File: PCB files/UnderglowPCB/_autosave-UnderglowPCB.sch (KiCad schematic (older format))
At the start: 67 parts, among them J1 USB_B_Micro, J12 DB9_Male, J4 Conn_01x07, J5 Conn_01x05, J7 Screw_Terminal_01x03, J8 Screw_Terminal_01x03, Q1 S8050, Q2 S8050, SW1 SW_Push, U1 CP2102N-A01-GQFN28, U2 TPS62133, U3 74HC14, U4 74HC14, U5 LD56100DPU33R, U6 ESP32-WROOM-32D, U7 SN65HVD230, U8 USBLC6-2SC6

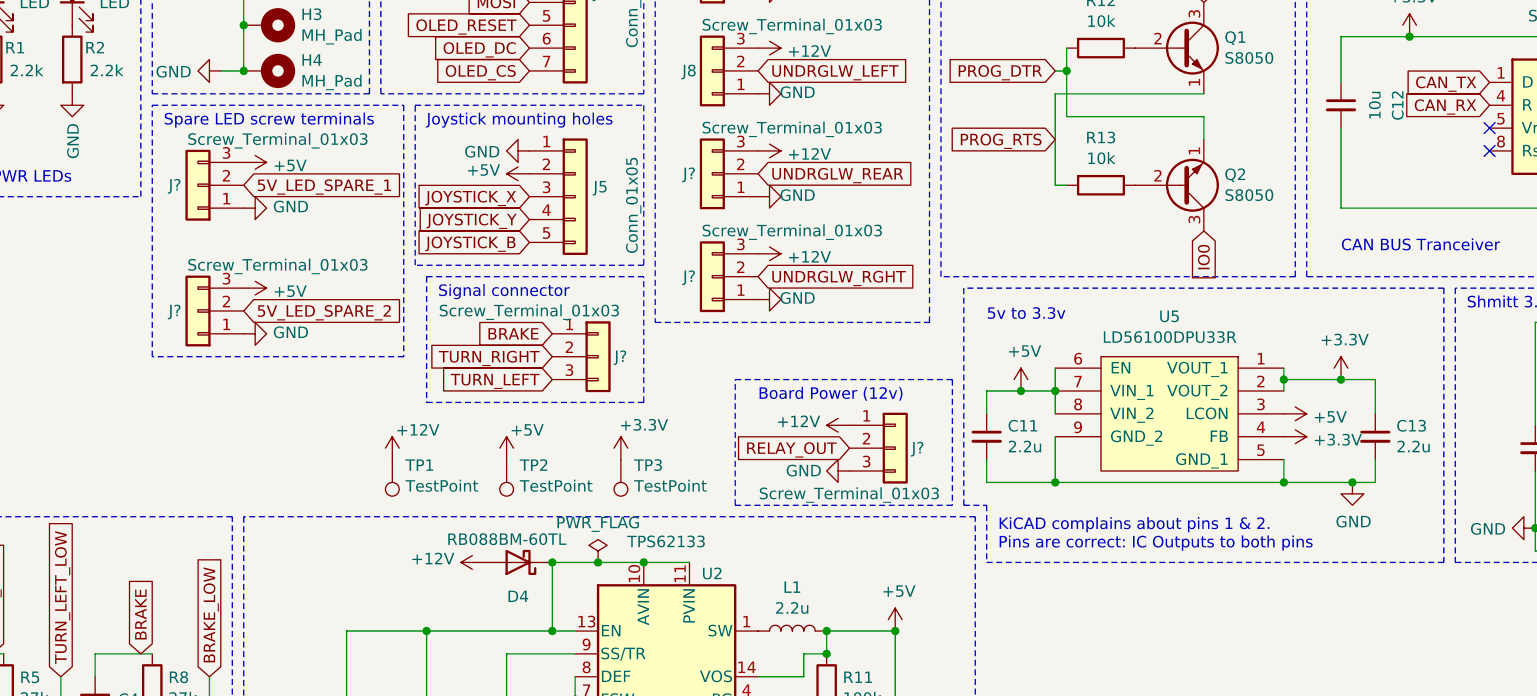
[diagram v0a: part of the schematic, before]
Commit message: Schemtic refined, removed screw terminals, added USB ESD prtection, test points, adjusted paths.
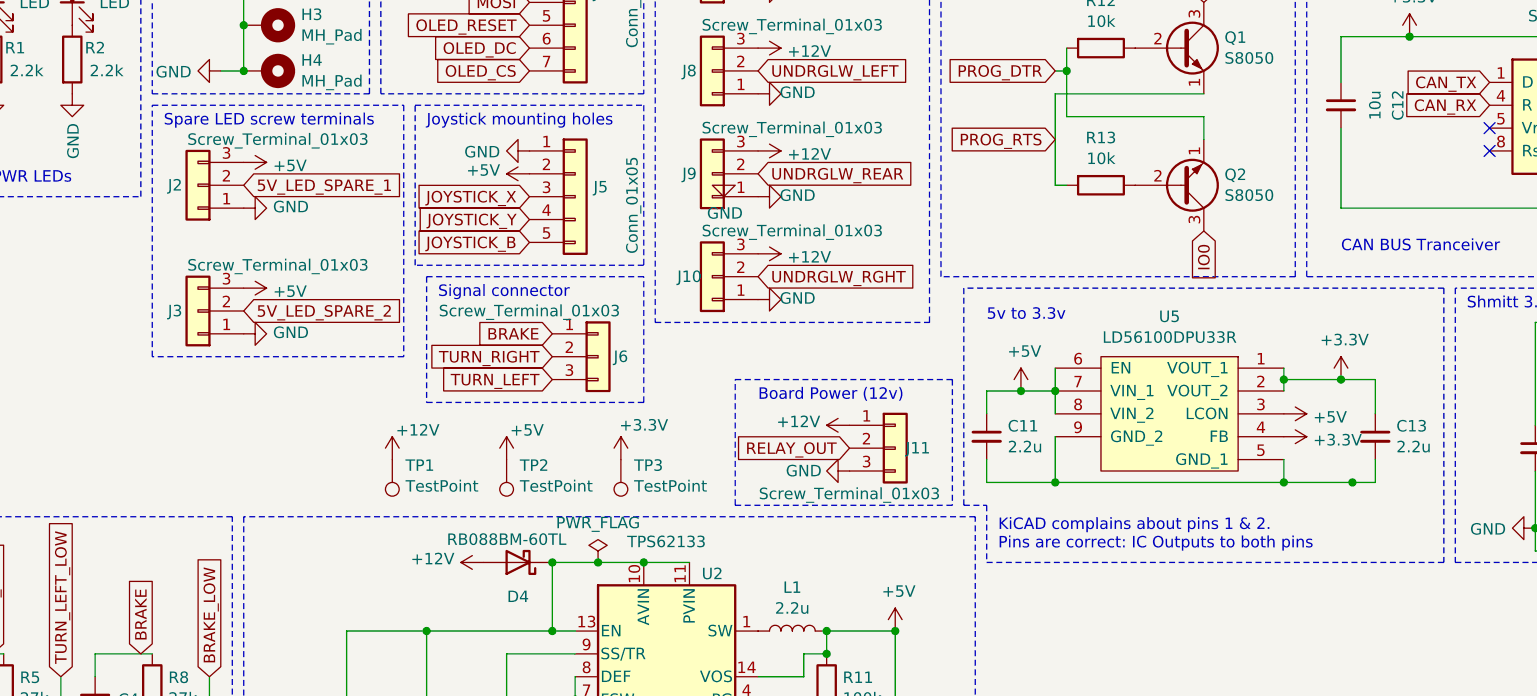
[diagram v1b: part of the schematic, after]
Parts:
- J10, J11, J3, J6, J9: renamed from J?; footprint TerminalBlock_Phoenix:TerminalBlock_Phoenix_MKDS-1,5-3-5.08_1x03_P5.08mm_Horizontal -> Connector_PinHeader_2.54mm:PinHeader_1x03_P2.54mm_Vertical
- J2: renamed from J?; footprint TerminalBlock_Phoenix:TerminalBlock_Phoenix_MKDS-1,5-3-5.08_1x03_P5.08mm_Horizontal -> Connector_PinSocket_2.54mm:PinSocket_1x03_P2.54mm_Vertical
- J7, J8: footprint TerminalBlock_Phoenix:TerminalBlock_Phoenix_MKDS-1,5-3-5.08_1x03_P5.08mm_Horizontal -> Connector_PinHeader_2.54mm:PinHeader_1x03_P2.54mm_Vertical
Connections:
- net GND: no longer C11.2, C13.2, U5.5 (GND_1), U5.9 (GND_2)
- new net: C11.2, C13.2, U5.5 (GND_1), U5.9 (GND_2)
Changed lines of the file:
@@
 L power:GND #PWR017
 U 1 1 606E5808
-P 7900 6400
-F 0 "#PWR017" H 7900 6150 50  0001 C CNN
-F 1 "GND" H 7905 6227 50  0000 C CNN
-F 2 "" H 7900 6400 50  0001 C CNN
-F 3 "" H 7900 6400 50  0001 C CNN
-	1    7900 6400
+P 5150 5050
+F 0 "#PWR017" H 5150 4800 50  0001 C CNN
+F 1 "GND" H 5155 4877 50  0000 C CNN
+F 2 "" H 5150 5050 50  0001 C CNN
+F 3 "" H 5150 5050 50  0001 C CNN
+	1    5150 5050
 	1    0    0    -1
 $EndComp
@@
 F 0 "J7" H 5200 4150 50  0000 C CNN
 F 1 "Screw_Terminal_01x03" H 4750 3950 50  0000 C CNN
-F 2 "TerminalBlock_Phoenix:TerminalBlock_Phoenix_MKDS-1,5-3-5.08_1x03_P5.08mm_Horizontal" H 5100 4150 50  0001 C CNN
+F 2 "Connector_PinHeader_2.54mm:PinHeader_1x03_P2.54mm_Vertical" H 5100 4150 50  0001 C CNN
 F 3 "~" H 5100 4150 50  0001 C CNN
 	1    5100 4150
@@
 F 0 "J8" H 5200 4600 50  0000 C CNN
 F 1 "Screw_Terminal_01x03" H 4750 4400 50  0000 C CNN
-F 2 "TerminalBlock_Phoenix:TerminalBlock_Phoenix_MKDS-1,5-3-5.08_1x03_P5.08mm_Horizontal" H 5100 4600 50  0001 C CNN
+F 2 "Connector_PinHeader_2.54mm:PinHeader_1x03_P2.54mm_Vertical" H 5100 4600 50  0001 C CNN
 F 3 "~" H 5100 4600 50  0001 C CNN
 	1    5100 4600
@@
 $EndComp
 $Comp
-L Connector_Generic:Conn_01x03 J?
+L Connector_Generic:Conn_01x03 J9
 U 1 1 60AA5191
 P 5100 5050
-F 0 "J?" H 5200 5050 50  0000 C CNN
+F 0 "J9" H 5200 5050 50  0000 C CNN
 F 1 "Screw_Terminal_01x03" H 4750 4850 50  0000 C CNN
-F 2 "TerminalBlock_Phoenix:TerminalBlock_Phoenix_MKDS-1,5-3-5.08_1x03_P5.08mm_Horizontal" H 5100 5050 50  0001 C CNN
+F 2 "Connector_PinHeader_2.54mm:PinHeader_1x03_P2.54mm_Vertical" H 5100 5050 50  0001 C CNN
 F 3 "~" H 5100 5050 50  0001 C CNN
 	1    5100 5050
@@
 $EndComp
 $Comp
-L Connector_Generic:Conn_01x03 J?
+L Connector_Generic:Conn_01x03 J10
 U 1 1 60AA6F94
 P 5100 5500
-F 0 "J?" H 5200 5500 50  0000 C CNN
+F 0 "J10" H 5200 5500 50  0000 C CNN
 F 1 "Screw_Terminal_01x03" H 4750 5300 50  0000 C CNN
-F 2 "TerminalBlock_Phoenix:TerminalBlock_Phoenix_MKDS-1,5-3-5.08_1x03_P5.08mm_Horizontal" H 5100 5500 50  0001 C CNN
+F 2 "Connector_PinHeader_2.54mm:PinHeader_1x03_P2.54mm_Vertical" H 5100 5500 50  0001 C CNN
 F 3 "~" H 5100 5500 50  0001 C CNN
 	1    5100 5500
@@
 $EndComp
 $Comp
-L Connector_Generic:Conn_01x03 J?
+L Connector_Generic:Conn_01x03 J2
 U 1 1 60AA8534
 P 2850 5100
-F 0 "J?" H 2950 5100 50  0000 C CNN
+F 0 "J2" H 2950 5100 50  0000 C CNN
 F 1 "Screw_Terminal_01x03" H 2500 4900 50  0000 C CNN
-F 2 "TerminalBlock_Phoenix:TerminalBlock_Phoenix_MKDS-1,5-3-5.08_1x03_P5.08mm_Horizontal" H 2850 5100 50  0001 C CNN
+F 2 "Connector_PinSocket_2.54mm:PinSocket_1x03_P2.54mm_Vertical" H 2850 5100 50  0001 C CNN
 F 3 "~" H 2850 5100 50  0001 C CNN
 	1    2850 5100
@@
 $EndComp
 $Comp
-L Connector_Generic:Conn_01x03 J?
+L Connector_Generic:Conn_01x03 J3
 U 1 1 60AA9C69
 P 2850 5650
-F 0 "J?" H 2950 5650 50  0000 C CNN
+F 0 "J3" H 2950 5650 50  0000 C CNN
 F 1 "Screw_Terminal_01x03" H 2500 5450 50  0000 C CNN
-F 2 "TerminalBlock_Phoenix:TerminalBlock_Phoenix_MKDS-1,5-3-5.08_1x03_P5.08mm_Horizontal" H 2850 5650 50  0001 C CNN
+F 2 "Connector_PinHeader_2.54mm:PinHeader_1x03_P2.54mm_Vertical" H 2850 5650 50  0001 C CNN
 F 3 "~" H 2850 5650 50  0001 C CNN
 	1    2850 5650
@@
 $EndComp
 $Comp
-L Connector_Generic:Conn_01x03 J?
+L Connector_Generic:Conn_01x03 J6
 U 1 1 60AAB3C9
 P 4600 5850
-F 0 "J?" H 4700 5850 50  0000 C CNN
+F 0 "J6" H 4700 5850 50  0000 C CNN
 F 1 "Screw_Terminal_01x03" H 4300 6050 50  0000 C CNN
-F 2 "TerminalBlock_Phoenix:TerminalBlock_Phoenix_MKDS-1,5-3-5.08_1x03_P5.08mm_Horizontal" H 4600 5850 50  0001 C CNN
+F 2 "Connector_PinHeader_2.54mm:PinHeader_1x03_P2.54mm_Vertical" H 4600 5850 50  0001 C CNN
 F 3 "~" H 4600 5850 50  0001 C CNN
 	1    4600 5850
@@
 $EndComp
 $Comp
-L Connector_Generic:Conn_01x03 J?
+L Connector_Generic:Conn_01x03 J11
 U 1 1 60AACEEC
 P 5900 6250
-F 0 "J?" H 6000 6250 50  0000 C CNN
+F 0 "J11" H 6000 6250 50  0000 C CNN
 F 1 "Screw_Terminal_01x03" H 5700 6050 50  0000 C CNN
-F 2 "TerminalBlock_Phoenix:TerminalBlock_Phoenix_MKDS-1,5-3-5.08_1x03_P5.08mm_Horizontal" H 5900 6250 50  0001 C CNN
+F 2 "Connector_PinHeader_2.54mm:PinHeader_1x03_P2.54mm_Vertical" H 5900 6250 50  0001 C CNN
 F 3 "~" H 5900 6250 50  0001 C CNN
 	1    5900 6250
